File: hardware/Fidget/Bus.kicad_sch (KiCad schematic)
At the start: 7 parts

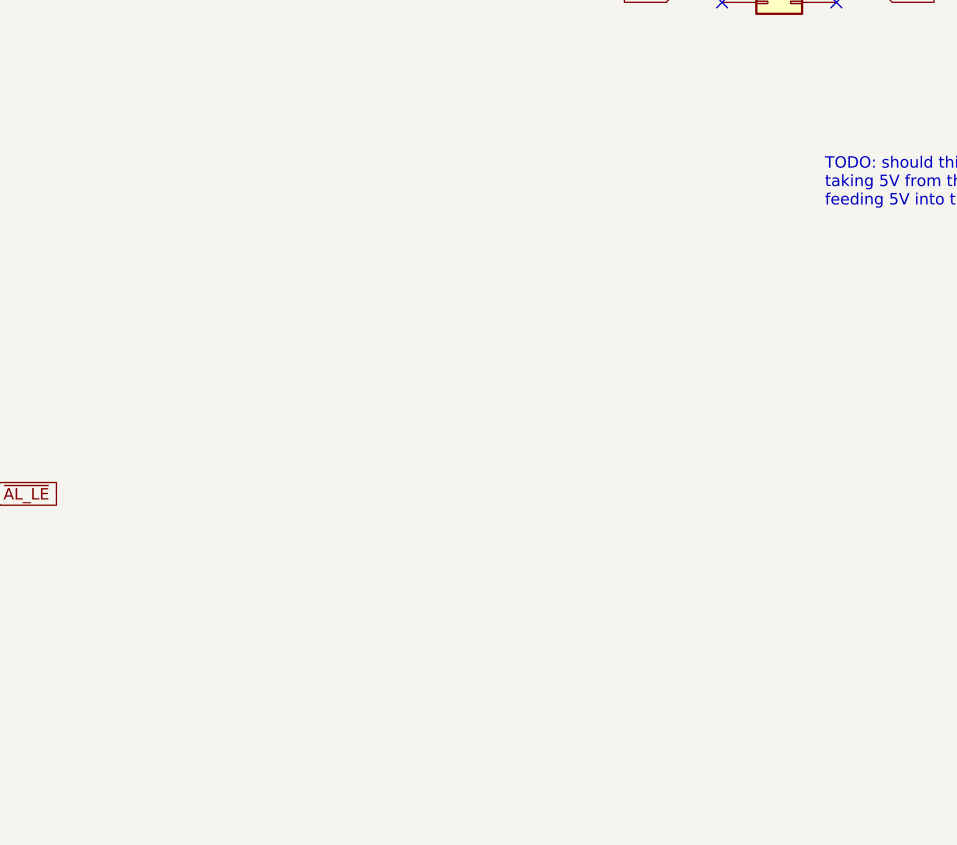
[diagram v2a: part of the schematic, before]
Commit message: Progress on sorting out the transceiver controls
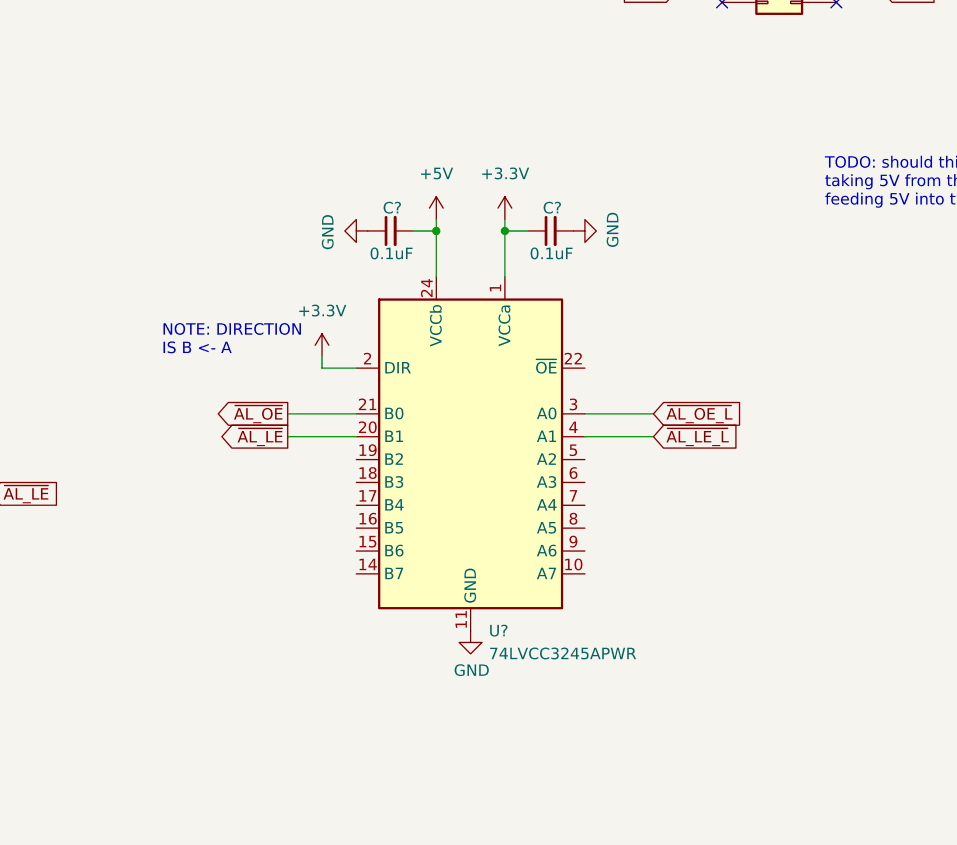
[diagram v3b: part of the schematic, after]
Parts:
- added C? (x2): 0.1uF, symbol Device:C_Small
- added U?: 74LVCC3245APWR, Package_SO:TSSOP-24_4.4x7.8mm_P0.65mm, symbol Fidget:74LVCC3245APWR
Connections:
- net +5V: now also C?.2, U?.24 (VCCb)
- net GND: now also C?.1, C?.2, U?.11 (GND), U?.12 (GND), U?.13 (GND)
- net ~{AL_LE}: now also U?.20 (B1)
- net ~{AL_OE}: now also U?.21 (B0)
- new net +3.3V: C?.1, U?.1 (VCCa), U?.2 (DIR)
- new net ~{AL_LE_L}: U?.4 (A1)
- new net ~{AL_OE_L}: U?.3 (A0)
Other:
- note added: "NOTE: DIRECTION IS B <- A"

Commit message: Added jumper to select bus voltage
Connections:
- net +5V: no longer C?.2, U?.24 (VCCb)
- new net VBUS: C?.2, U?.24 (VCCb)
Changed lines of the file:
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@@
     )
-  )
-  (symbol (lib_id "power:+5V") (at 152.4 104.14 0) (unit 1)
-    (in_bom yes) (on_board yes) (fields_autoplaced)
-    (property "Reference" "#PWR?" (id 0) (at 152.4 107.95 0)
-      (effects (font (size 1.27 1.27)) hide)
-    )
-    (property "Value" "+5V" (id 1) (at 152.4 99.06 0))
-    (property "Footprint" "" (id 2) (at 152.4 104.14 0)
-      (effects (font (size 1.27 1.27)) hide)
-    )
-    (property "Datasheet" "" (id 3) (at 152.4 104.14 0)
-      (effects (font (size 1.27 1.27)) hide)
-    )
-    (pin "1")
   )
   (symbol (lib_id "power:+5V") (at 76.2 40.64 0) (unit 1)
@@
       (effects (font (size 1.27 1.27)) hide)
     )
+    (pin "1")
+  )
+  (symbol (lib_id "power:VBUS") (at 152.4 104.14 0) (unit 1)
+    (in_bom yes) (on_board yes) (fields_autoplaced)
+    (property "Reference" "#PWR?" (id 0) (at 152.4 107.95 0)
+      (effects (font (size 1.27 1.27)) hide)
+    )
+    (property "Value" "VBUS" (id 1) (at 152.4 99.06 0))
+    (property "Footprint" "" (id 2) (at 152.4 104.14 0)
+      (effects (font (size 1.27 1.27)) hide)
+    )
+    (property "Datasheet" "" (id 3) (at 152.4 104.14 0)
+      (effects (font (size 1.27 1.27)) hide)
+    )

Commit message: Filled in more details in schematic
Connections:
- net GND: now also U?.22 (~{OE})
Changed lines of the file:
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@@
   (symbol (lib_id "power:+5V") (at 76.2 40.64 0) (unit 1)
     (in_bom yes) (on_board yes) (fields_autoplaced)
-    (property "Reference" "#PWR?" (id 0) (at 76.2 44.45 0)
+    (property "Reference" "#PWR0190" (id 0) (at 76.2 44.45 0)
       (effects (font (size 1.27 1.27)) hide)
     )
@@
     (pin "1")
   )
+  (symbol (lib_id "power:GND") (at 168.91 120.65 90) (unit 1)
+    (in_bom yes) (on_board yes)
+    (property "Reference" "#PWR0196" (id 0) (at 175.26 120.65 0)
+      (effects (font (size 1.27 1.27)) hide)
+    )
+    (property "Value" "GND" (id 1) (at 173.3042 120.523 0))
+    (property "Footprint" "" (id 2) (at 168.91 120.65 0)
+      (effects (font (size 1.27 1.27)) hide)
+    )
+    (property "Datasheet" "" (id 3) (at 168.91 120.65 0)
+      (effects (font (size 1.27 1.27)) hide)
+    )
+    (pin "1")
+  )
   (symbol (lib_id "power:+3.3V") (at 139.7 119.38 0) (unit 1)
     (in_bom yes) (on_board yes) (fields_autoplaced)
-    (property "Reference" "#PWR?" (id 0) (at 139.7 123.19 0)
+    (property "Reference" "#PWR0199" (id 0) (at 139.7 123.19 0)
       (effects (font (size 1.27 1.27)) hide)
     )
@@
   (symbol (lib_id "power:VBUS") (at 152.4 104.14 0) (unit 1)
     (in_bom yes) (on_board yes) (fields_autoplaced)
-    (property "Reference" "#PWR?" (id 0) (at 152.4 107.95 0)
+    (property "Reference" "#PWR0198" (id 0) (at 152.4 107.95 0)
       (effects (font (size 1.27 1.27)) hide)
     )
@@
   (symbol (lib_id "power:+5V") (at 76.2 120.65 0) (unit 1)
     (in_bom yes) (on_board yes) (fields_autoplaced)
-    (property "Reference" "#PWR?" (id 0) (at 76.2 124.46 0)
+    (property "Reference" "#PWR0194" (id 0) (at 76.2 124.46 0)
       (effects (font (size 1.27 1.27)) hide)
     )
@@
   (symbol (lib_id "power:GND") (at 76.2 185.42 0) (unit 1)
     (in_bom yes) (on_board yes)
-    (property "Reference" "#PWR?" (id 0) (at 76.2 191.77 0)
+    (property "Reference" "#PWR0191" (id 0) (at 76.2 191.77 0)
       (effects (font (size 1.27 1.27)) hide)
     )
@@
   (symbol (lib_id "power:GND") (at 68.58 41.91 270) (unit 1)
     (in_bom yes) (on_board yes)
-    (property "Reference" "#PWR?" (id 0) (at 62.23 41.91 0)
+    (property "Reference" "#PWR0189" (id 0) (at 62.23 41.91 0)
       (effects (font (size 1.27 1.27)) hide)
     )
@@
   (symbol (lib_id "power:GND") (at 156.21 149.86 0) (unit 1)
     (in_bom yes) (on_board yes)
-    (property "Reference" "#PWR?" (id 0) (at 156.21 156.21 0)
+    (property "Reference" "#PWR0195" (id 0) (at 156.21 156.21 0)
       (effects (font (size 1.27 1.27)) hide)
     )
@@
   (symbol (lib_id "power:GND") (at 167.64 105.41 90) (unit 1)
     (in_bom yes) (on_board yes)
-    (property "Reference" "#PWR?" (id 0) (at 173.99 105.41 0)
+    (property "Reference" "#PWR0200" (id 0) (at 173.99 105.41 0)
       (effects (font (size 1.27 1.27)) hide)
     )
@@
   (symbol (lib_id "power:GND") (at 76.2 105.41 0) (unit 1)
     (in_bom yes) (on_board yes)
-    (property "Reference" "#PWR?" (id 0) (at 76.2 111.76 0)
+    (property "Reference" "#PWR0192" (id 0) (at 76.2 111.76 0)
       (effects (font (size 1.27 1.27)) hide)
     )
@@
   (symbol (lib_id "power:+3.3V") (at 160.02 104.14 0) (unit 1)
     (in_bom yes) (on_board yes) (fields_autoplaced)
-    (property "Reference" "#PWR?" (id 0) (at 160.02 107.95 0)
+    (property "Reference" "#PWR0201" (id 0) (at 160.02 107.95 0)
       (effects (font (size 1.27 1.27)) hide)
     )
@@
   (symbol (lib_id "power:GND") (at 144.78 105.41 270) (unit 1)
     (in_bom yes) (on_board yes)
-    (property "Reference" "#PWR?" (id 0) (at 138.43 105.41 0)
+    (property "Reference" "#PWR0197" (id 0) (at 138.43 105.41 0)
       (effects (font (size 1.27 1.27)) hide)
     )
@@
   (symbol (lib_id "power:GND") (at 68.58 121.92 270) (unit 1)
     (in_bom yes) (on_board yes)
-    (property "Reference" "#PWR?" (id 0) (at 62.23 121.92 0)
-      (effects (font (size 1.27 1.27)) hide)
-    )
+    (property "Reference" "#PWR0193" (id 0) (at 62.23 121.92 0)
+      (effects (font (size 1.27 1.27)) hide)
+    )

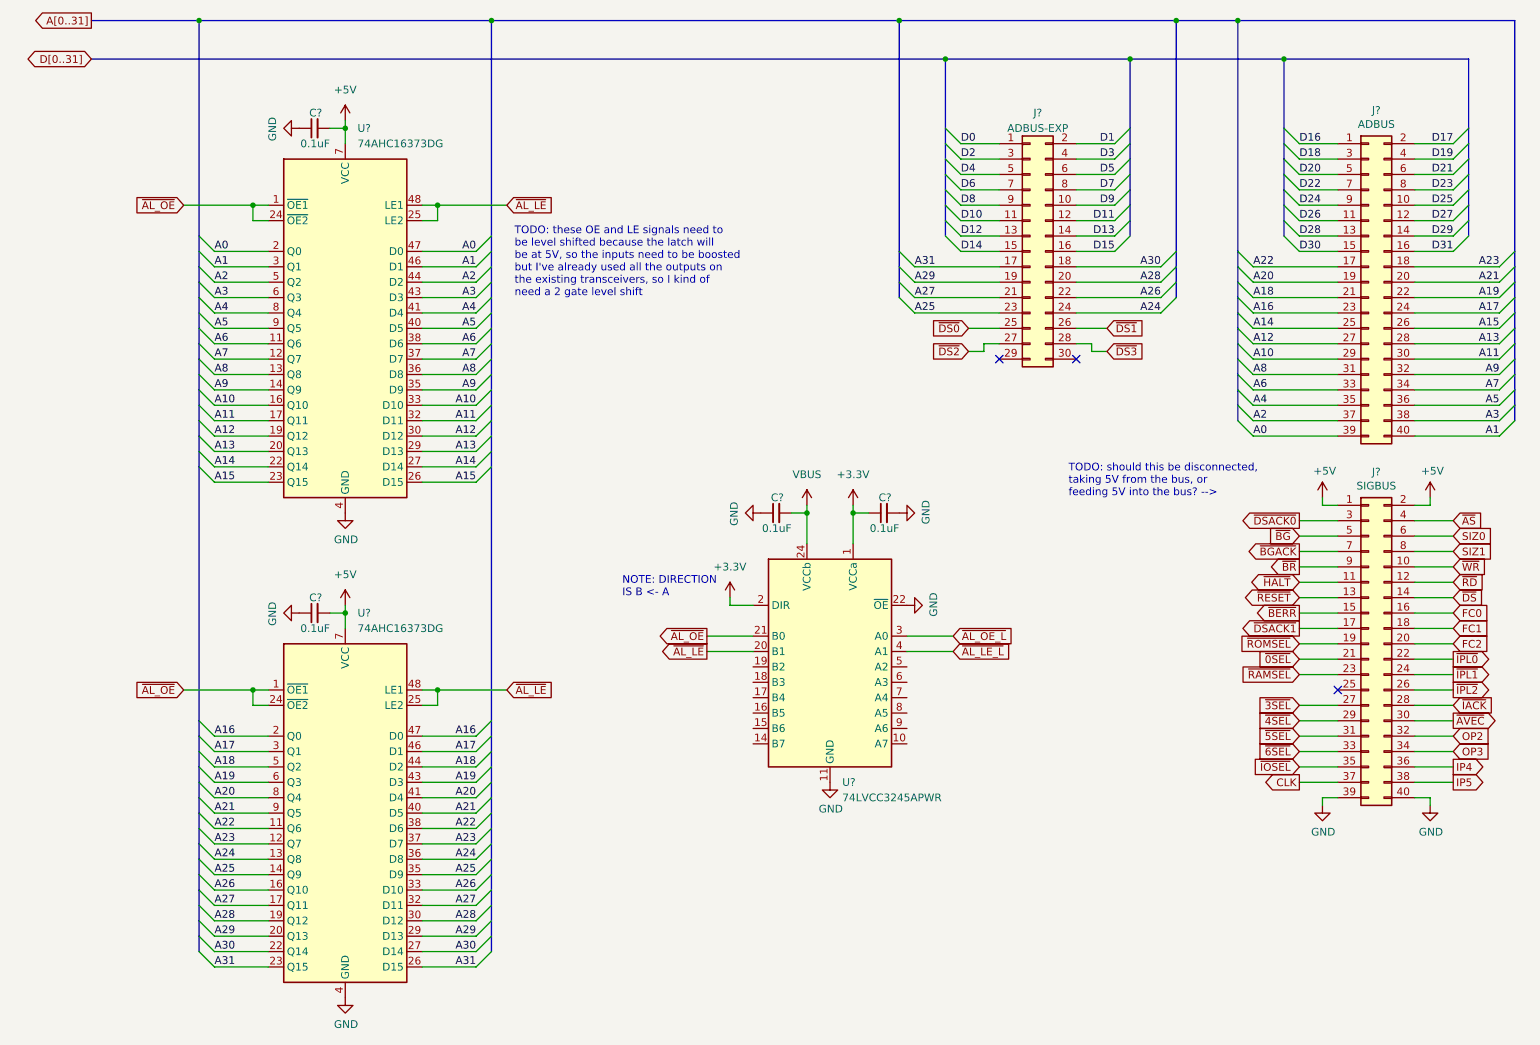
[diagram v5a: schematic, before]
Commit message: Minor updates, and start of PCB layout
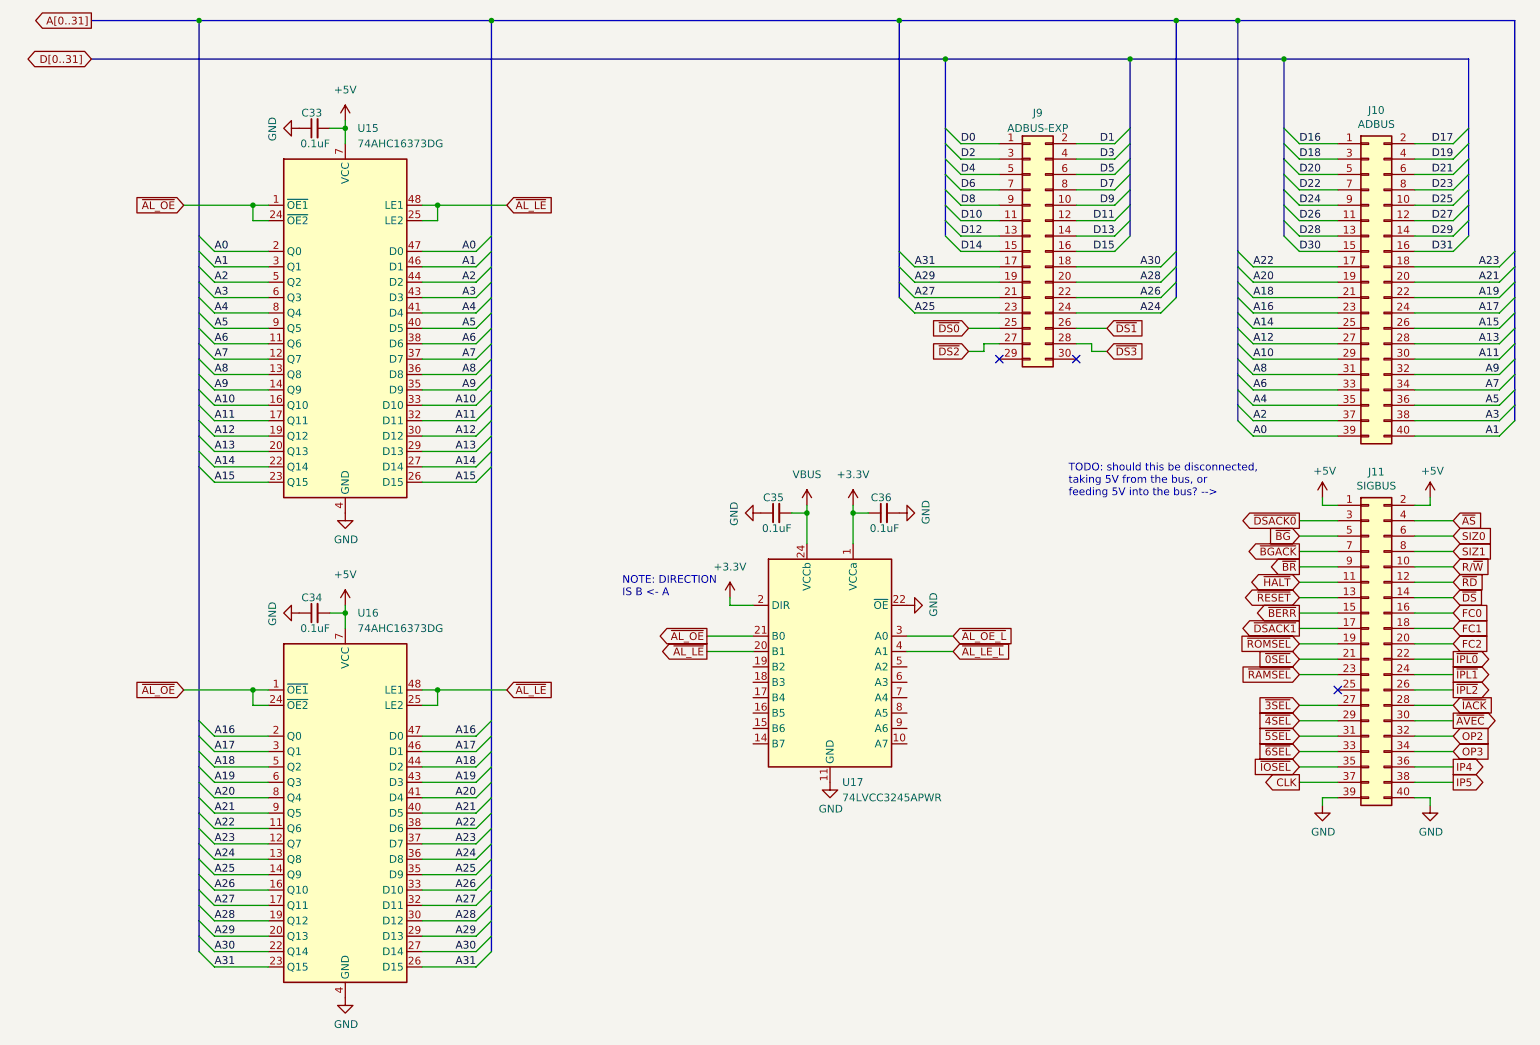
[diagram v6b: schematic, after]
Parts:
- C33, C34, C35, C36: renamed from C?; footprint (none) -> Capacitor_SMD:C_0805_2012Metric_Pad1.18x1.45mm_HandSolder
- gave numbers to parts that had none: 6
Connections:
- net ~{WR} renamed R/~{W}
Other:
- note removed: "TODO: these OE and LE signals need to be level shifted because the latch will be at 5V, so the inputs need to be boosted but I've already used all the outputs on the existing transceivers, so I kind of need a 2 gate level shift"

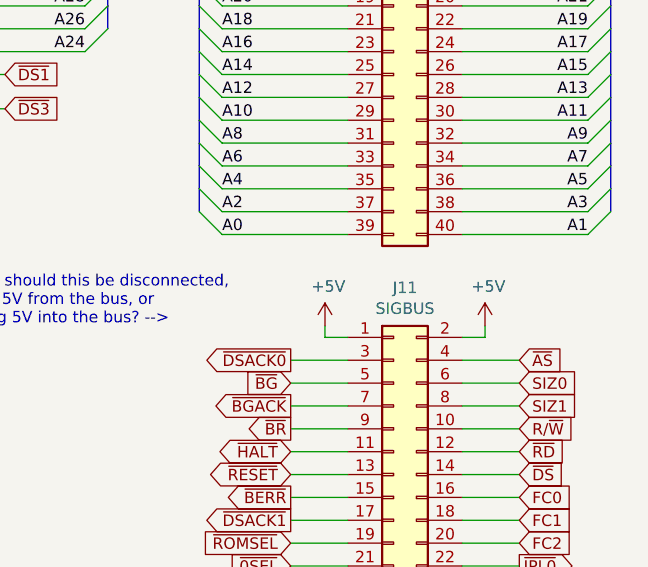
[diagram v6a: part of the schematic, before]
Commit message: More PCB layout and fixes and reassigments to the schematics
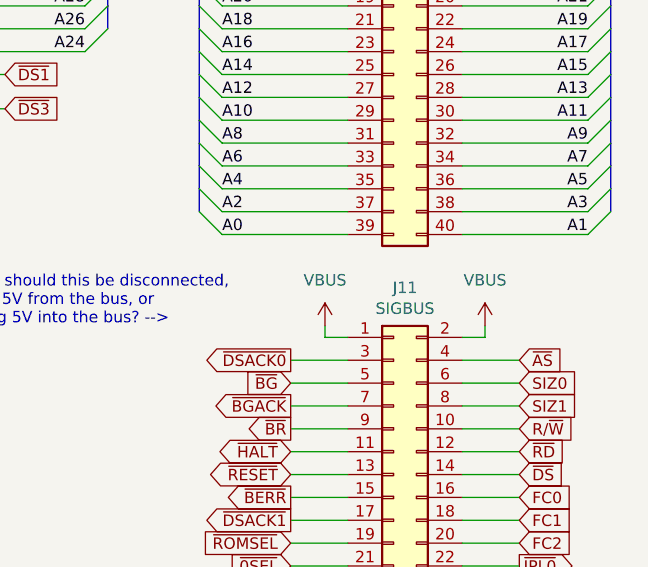
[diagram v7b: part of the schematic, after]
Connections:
- net +5V: no longer J11.1 (Pin_1), J11.2 (Pin_2)
- net VBUS: now also J11.1 (Pin_1), J11.2 (Pin_2)
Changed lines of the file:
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@@
     )
+  )
+  (symbol (lib_id "power:VBUS") (at 237.49 102.87 0) (unit 1)
+    (in_bom yes) (on_board yes) (fields_autoplaced)
+    (property "Reference" "#PWR?" (id 0) (at 237.49 106.68 0)
+      (effects (font (size 1.27 1.27)) hide)
+    )
+    (property "Value" "VBUS" (id 1) (at 237.49 97.79 0))
+    (property "Footprint" "" (id 2) (at 237.49 102.87 0)
+      (effects (font (size 1.27 1.27)) hide)
+    )
+    (property "Datasheet" "" (id 3) (at 237.49 102.87 0)
+      (effects (font (size 1.27 1.27)) hide)
+    )
+    (pin "1")
   )
   (symbol (lib_id "power:+5V") (at 76.2 40.64 0) (unit 1)
@@
     (pin "2")
   )
-  (symbol (lib_id "power:+5V") (at 237.49 102.87 0) (unit 1)
-    (in_bom yes) (on_board yes)
-    (property "Reference" "#PWR0121" (id 0) (at 237.49 106.68 0)
-      (effects (font (size 1.27 1.27)) hide)
-    )
-    (property "Value" "+5V" (id 1) (at 237.871 98.4758 0))
-    (property "Footprint" "" (id 2) (at 237.49 102.87 0)
-      (effects (font (size 1.27 1.27)) hide)
-    )
-    (property "Datasheet" "" (id 3) (at 237.49 102.87 0)
-      (effects (font (size 1.27 1.27)) hide)
-    )
-    (pin "1")
-  )
   (symbol (lib_id "Connector_Generic:Conn_02x20_Odd_Even") (at 245.11 67.31 0) (unit 1)
     (in_bom yes) (on_board yes)
@@
     )
     (property "Datasheet" "" (id 3) (at 160.02 104.14 0)
-      (effects (font (size 1.27 1.27)) hide)
-    )
-    (pin "1")
-  )
-  (symbol (lib_id "power:+5V") (at 255.27 102.87 0) (unit 1)
-    (in_bom yes) (on_board yes)
-    (property "Reference" "#PWR0122" (id 0) (at 255.27 106.68 0)
-      (effects (font (size 1.27 1.27)) hide)
-    )
-    (property "Value" "+5V" (id 1) (at 255.651 98.4758 0))
-    (property "Footprint" "" (id 2) (at 255.27 102.87 0)
-      (effects (font (size 1.27 1.27)) hide)
-    )
-    (property "Datasheet" "" (id 3) (at 255.27 102.87 0)
       (effects (font (size 1.27 1.27)) hide)
     )
@@
       (effects (font (size 1.27 1.27)) hide)
     )
+    (pin "1")
+  )
+  (symbol (lib_id "power:VBUS") (at 255.27 102.87 0) (unit 1)
+    (in_bom yes) (on_board yes) (fields_autoplaced)
+    (property "Reference" "#PWR?" (id 0) (at 255.27 106.68 0)
+      (effects (font (size 1.27 1.27)) hide)
+    )
+    (property "Value" "VBUS" (id 1) (at 255.27 97.79 0))
+    (property "Footprint" "" (id 2) (at 255.27 102.87 0)
+      (effects (font (size 1.27 1.27)) hide)
+    )
+    (property "Datasheet" "" (id 3) (at 255.27 102.87 0)
+      (effects (font (size 1.27 1.27)) hide)
+    )

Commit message: Almost done Rev1 board design
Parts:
- added JP8: BUS POWER, Connector_PinHeader_2.54mm:PinHeader_1x02_P2.54mm_Vertical, symbol Jumper:Jumper_2_Bridged
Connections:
- net +5V is gone; now on net VBUS: C33.2, C34.2, U15.18 (VCC), U15.31 (VCC), U15.42 (VCC), U15.7 (VCC), U16.18 (VCC), U16.31 (VCC), U16.42 (VCC), U16.7 (VCC)
- net VBUS: now also JP8.1 (A); no longer J11.1 (Pin_1), J11.2 (Pin_2)
- net IP4: no longer names the net of J11.36 (Pin_36)
- net IP5: no longer names the net of J11.38 (Pin_38)
- net OP2: no longer names the net of J11.32 (Pin_32)
- net OP3: no longer names the net of J11.34 (Pin_34)
- net ~{0SEL}: no longer names the net of J11.21 (Pin_21)
- net ~{3SEL}: no longer names the net of J11.27 (Pin_27)
- net ~{4SEL}: no longer names the net of J11.29 (Pin_29)
- net ~{5SEL}: no longer names the net of J11.31 (Pin_31)
- net ~{6SEL}: no longer names the net of J11.33 (Pin_33)
- net ~{DS0}: no longer names the net of J9.25 (Pin_25)
- net ~{DS1}: no longer names the net of J9.26 (Pin_26)
- net ~{DS2}: no longer names the net of J9.27 (Pin_27)
- net ~{DS3}: no longer names the net of J9.28 (Pin_28)
- net ~{IOSEL}: no longer names the net of J11.35 (Pin_35)
- net ~{RAMSEL}: no longer names the net of J11.23 (Pin_23)
- net ~{RD}: no longer names the net of J11.12 (Pin_12)
- net ~{ROMSEL}: no longer names the net of J11.19 (Pin_19)
- new net: J11.1 (Pin_1), J11.2 (Pin_2), JP8.2 (B)
- no-connect marks 3 -> 32
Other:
- note removed: "TODO: should this be disconnected, taking 5V from the bus, or feeding 5V into the bus? -->"
